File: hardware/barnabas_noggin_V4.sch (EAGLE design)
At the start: 45 parts, among them IC2 LM1117IMPX-5.0, IC3 ATMEGA328P-32MUR, J1 POWER_JACKPTH, J3 USB-mini-90 -SMD, J4 ICSP, SW1 157SW, Y1 16MHZ, Y2 12MHz

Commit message: Updated V4 schematics.
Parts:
- removed F1: FUSE_6V, barnabas_noggin_V4:FUSE_6V
- added F2: FUSE_6V, barnabas_noggin_V4:FUSE_6V
- added JP7: 2.54mm, barnabas_noggin_V4:PINHD-1X6
- added M1, M2, M3, M4: MOUNT_HOLE, barnabas_noggin_V4:MOUNT_HOLE
- added R7, R8, R9: 1K, barnabas_noggin_V4:RESISTOR0603
- added SW2: 157SW, barnabas_noggin_V4:PUSHBUTTON
- added U1: L9110S_DRIVER, barnabas_noggin_V4:L9110S_DRIVER
- R4: device barnabas_noggin_V4:RESISTORX4 -> barnabas_noggin_V4:RESISTOR0603; PARTNO CAY16-102J4LF -> RC0603FR-071KL
- renumbered U$1 to IC1
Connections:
- removed net COM: C4.2, IC1.GND
- removed net N$11: L.A, R4D.1
- removed net N$15: F1.1, J3.VBUS
- new net 5V_PIN: C11.1, C12.1, C13.1, C14.1, C3.1, C5.+, C7.1, F2.2, IC1.VCC, IC3.AVCC, IC3.VCC@1, IC3.VCC@2, J4.2, JP1.3, JP1.4, JP2.3, JP2.4, JP6.4, R1.2, R7.2, R8.2, R9.2
- new net N$10: L.A, R4.1
- net 5V: now also F2.1; no longer C11.1, C12.1, C13.1, C14.1, C3.1, C5.+, C7.1, IC1.VCC, IC3.AVCC, IC3.VCC@1, IC3.VCC@2, J4.2, JP1.3, JP1.4, JP2.3, JP2.4, JP6.4, R1.2, R4A.2, R4B.2
- net D12/MISO: now also JP7.1
- net D13/SCK: now also R4.2; no longer R4D.2
- net D2: now also SW2.1
- net GND: now also C4.2, IC1.GND, SW2.2
- net N$3: now also R7.1; no longer R4C.1
- net N$7: now also R8.1; no longer R4A.1
- net N$9: now also R9.1; no longer R4B.1
- net VOUT: no longer R4C.2
- net VUSB: now also J3.VBUS; no longer F1.2
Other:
- note added: "DC Driver Connector"
- moved on the sheet: C4, D1, D2, JP3, JP4, JP5, JP6, PWR

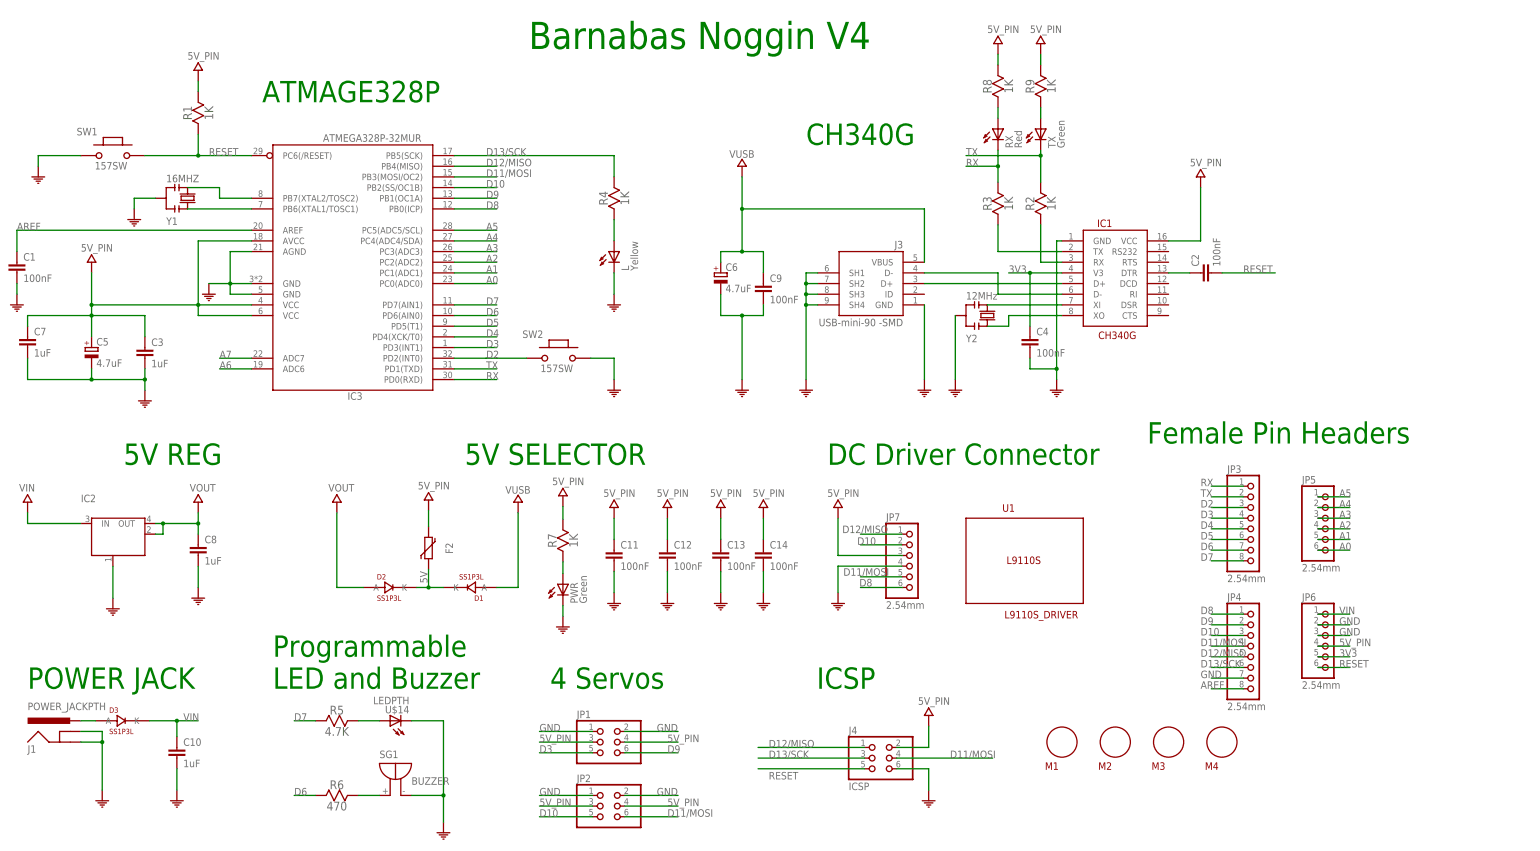
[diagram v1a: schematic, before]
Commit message: Added 3.3V regulator.
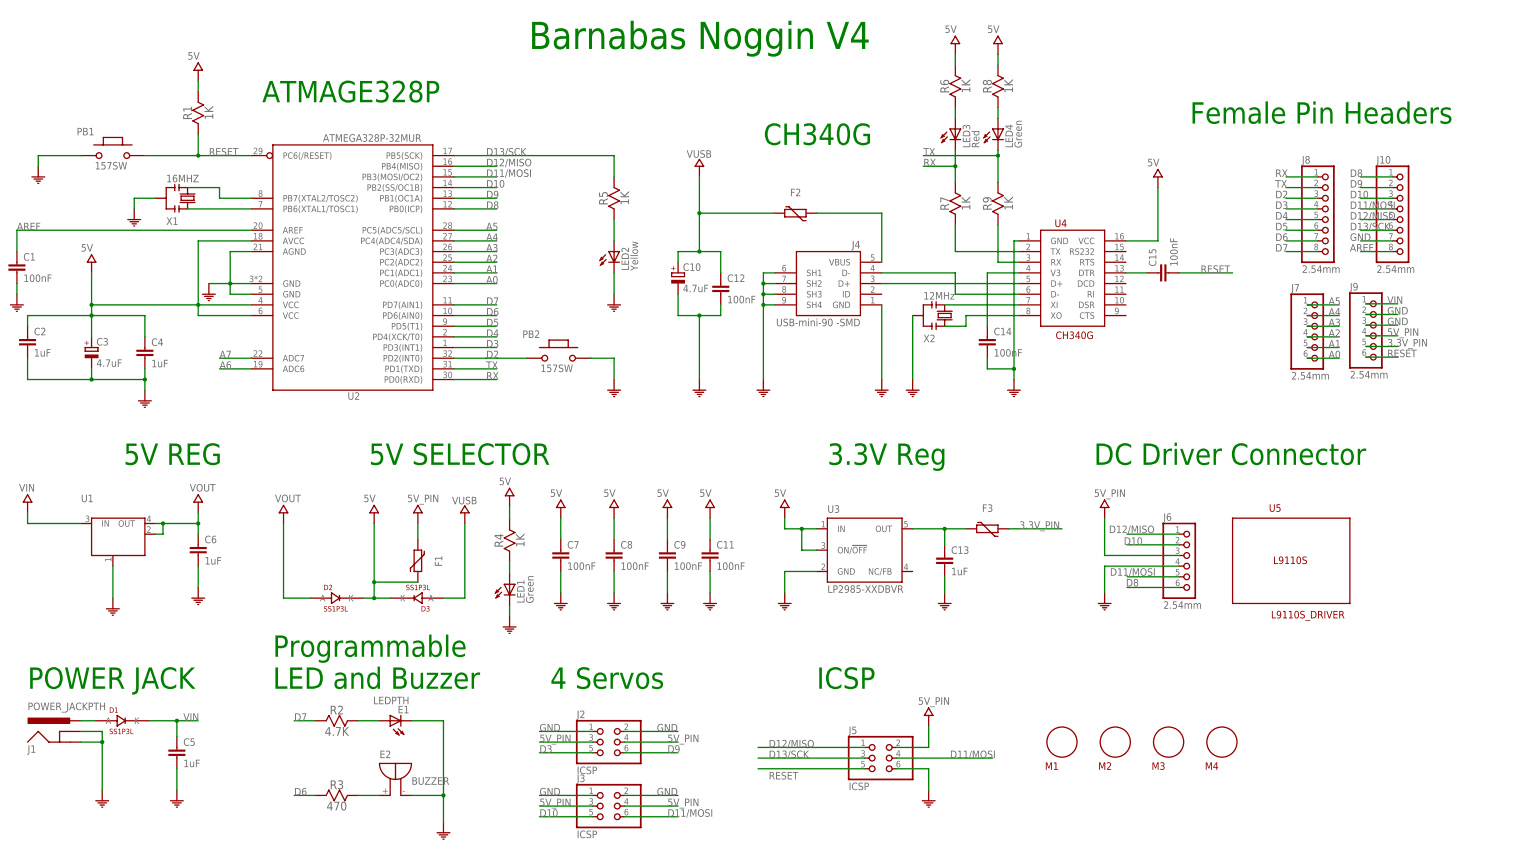
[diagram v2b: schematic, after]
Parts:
- removed IC1: CH340G, barnabas_noggin_V4:CH340G
- removed IC2: LM1117IMPX-5.0, barnabas_noggin_V4:LM1117
- removed JP2: (no value), barnabas_noggin_V4:CONNECTOR_2X3
- removed JP3, JP4: 2.54mm, barnabas_noggin_V4:PINHD-1X8
- removed JP5, JP6, JP7: 2.54mm, barnabas_noggin_V4:PINHD-1X6
- removed PWR, TX: Green, barnabas_noggin_V4:LED_GREEN
- removed RX: Red, barnabas_noggin_V4:LED_RED
- removed Y2: 12MHz, barnabas_noggin_V4:CRYSTAL_12MHZ
- added C15: 100nF, barnabas_noggin_V4:CAPACITOR_100NF_0603
- added F1, F3: FUSE_6V, barnabas_noggin_V4:FUSE_6V
- added J10, J8: 2.54mm, barnabas_noggin_V4:PINHD-1X8
- added J5: ICSP, barnabas_noggin_V4:CONNECTOR_2X3
- added J6, J7, J9: 2.54mm, barnabas_noggin_V4:PINHD-1X6
- added LED1, LED4: Green, barnabas_noggin_V4:LED_GREEN
- added LED3: Red, barnabas_noggin_V4:LED_RED
- added U3: LP2985-XXDBVR, barnabas_noggin_V4:LP2985-XXDBVR
- added U4: CH340G, barnabas_noggin_V4:CH340G
- added U5: L9110S_DRIVER, barnabas_noggin_V4:L9110S_DRIVER
- added X2: 12MHz, barnabas_noggin_V4:CRYSTAL_12MHZ
- C10, C3: value 1uF -> 4.7uF; device barnabas_noggin_V4:CAPACITOR_1UF_0603 -> barnabas_noggin_V4:CAPACITOR_4.7UF; PARTNO CC0603KRX5R8BB105 -> CL31A475KOHNNNE
- C13, C2, C4: value 100nF -> 1uF; device barnabas_noggin_V4:CAPACITOR_100NF_0603 -> barnabas_noggin_V4:CAPACITOR_1UF_0603; PARTNO CC0603ZRY5V9BB104 -> CC0603KRX5R8BB105
- C5, C6: value 4.7uF -> 1uF; device barnabas_noggin_V4:CAPACITOR_4.7UF -> barnabas_noggin_V4:CAPACITOR_1UF_0603; PARTNO CL31A475KOHNNNE -> CC0603KRX5R8BB105
- C7, C8: value 1uF -> 100nF; device barnabas_noggin_V4:CAPACITOR_1UF_0603 -> barnabas_noggin_V4:CAPACITOR_100NF_0603; PARTNO CC0603KRX5R8BB105 -> CC0603ZRY5V9BB104
- J2: value (none) -> ICSP
- J3: value USB-mini-90 -SMD -> ICSP; device barnabas_noggin_V4:CONNECTOR_USB_MINI-B -> barnabas_noggin_V4:CONNECTOR_2X3
- J4: value ICSP -> USB-mini-90 -SMD; device barnabas_noggin_V4:CONNECTOR_2X3 -> barnabas_noggin_V4:CONNECTOR_USB_MINI-B
- R2: value 1K -> 4.7K; device barnabas_noggin_V4:RESISTOR0603 -> barnabas_noggin_V4:RESISTOR; PARTNO RC0603FR-071KL -> (none)
- R3: value 1K -> 470; device barnabas_noggin_V4:RESISTOR0603 -> barnabas_noggin_V4:RESISTOR; PARTNO RC0603FR-071KL -> (none)
- R5: value 4.7K -> 1K; device barnabas_noggin_V4:RESISTOR -> barnabas_noggin_V4:RESISTOR0603; PARTNO (none) -> RC0603FR-071KL
- R6: value 470 -> 1K; device barnabas_noggin_V4:RESISTOR -> barnabas_noggin_V4:RESISTOR0603; PARTNO (none) -> RC0603FR-071KL
- U1: value L9110S_DRIVER -> LM1117IMPX-5.0; device barnabas_noggin_V4:L9110S_DRIVER -> barnabas_noggin_V4:LM1117; PARTNO (none) -> LM1117IMPX-5.0/NOPB
- renumbered IC3 to U2, JP1 to J2, L to LED2, SG1 to E2, SW1 to PB1, SW2 to PB2, U$14 to E1, Y1 to X1
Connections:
- removed net 3V3: C4.1, IC1.V3, JP6.5
- new net 3.3V: C13.1, F3.2, U3.OUT
- new net 3.3V_PIN: F3.1, J9.5
- new net N$11: C14.1, U4.V3
- new net N$17: F2.1, J4.VBUS
- net 5V: now also C11.1, C2.1, C3.+, C4.1, C7.1, C8.1, C9.1, D3.K, F1.1, R1.2, R4.2, R6.2, R8.2, U2.AVCC, U2.VCC@1, U2.VCC@2, U3.IN, U3.ON/!OFF, U4.VCC; no longer D1.K, F2.1
- net 5V_PIN: now also F1.2, J3.3, J3.4, J5.2, J6.3, J9.4; no longer C11.1, C12.1, C13.1, C14.1, C3.1, C5.+, C7.1, F2.2, IC1.VCC, J4.2, JP2.3, JP2.4, JP6.4, R1.2, R7.2, R8.2, R9.2, U2.AVCC, U2.VCC@1, U2.VCC@2
- net A0: now also J7.6; no longer JP5.6
- net A1: now also J7.5; no longer JP5.5
- net A2: now also J7.4; no longer JP5.4
- net A3: now also J7.3; no longer JP5.3
- net A4: now also J7.2; no longer JP5.2
- net A5: now also J7.1; no longer JP5.1
- net AREF: now also J10.8; no longer JP4.8
- net D10: now also J10.3, J3.5, J6.2; no longer JP2.5, JP4.3
- net D11/MOSI: now also J10.4, J3.6, J5.4, J6.5; no longer J4.4, JP2.6, JP4.4
- net D12/MISO: now also J10.5, J5.1, J6.1; no longer J4.1, JP4.5, JP7.1
- net D13/SCK: now also J10.6, J5.3, R5.2; no longer J4.3, JP4.6, R4.2
- net D2: now also J8.3; no longer JP3.3
- net D3: now also J8.4; no longer JP3.4
- net D4: now also J8.5; no longer JP3.5
- net D5: now also J8.6; no longer JP3.6
- net D6: now also J8.7, R3.1; no longer JP3.7, R6.1
- net D7: now also J8.8, R2.1; no longer JP3.8, R5.1
- net D8: now also J10.1, J6.6; no longer JP4.1
- net D9: now also J10.2; no longer JP4.2
- net GND: now also C10.-, C2.2, C3.-, C5.2, C6.2, J10.7, J3.1, J3.2, J4.GND, J4.SH1, J4.SH2, J4.SH3, J4.SH4, J5.6, J6.4, J9.2, J9.3, LED1.C, U1.GND/ADJ, U3.GND, U4.GND, X2.2; no longer C10.2, C3.2, C5.-, C6.-, IC1.GND, IC2.GND/ADJ, J3.GND, J3.SH1, J3.SH2, J3.SH3, J3.SH4, J4.6, JP2.1, JP2.2, JP4.7, JP6.2, JP6.3, PWR.C, Y2.2
- net N$10: now also R5.1; no longer R4.1
- net N$12: now also U4.XO, X2.1; no longer IC1.XO, Y2.1
- net N$13: now also J4.D+, U4.D+; no longer IC1.D+, J3.D+
- net N$14: now also J4.D-, U4.D-; no longer IC1.D-, J3.D-
- net N$16: now also D1.A; no longer D3.A
- net N$18: now also R2.2; no longer R5.2
- net N$19: now also R3.2; no longer R6.2
- net N$3: now also LED1.A, R4.1; no longer PWR.A, R7.1
- net N$4: now also C15.1, U4.DTR; no longer C2.1, IC1.DTR
- net N$5: now also U4.XI, X2.3; no longer IC1.XI, Y2.3
- net N$6: now also R7.1, U4.TX; no longer IC1.TX, R3.1
- net N$7: now also LED3.A, R6.1; no longer R8.1, RX.A
- net N$8: now also R9.1, U4.RX; no longer IC1.RX, R2.1
- net N$9: now also LED4.A, R8.1; no longer R9.1, TX.A
- net RESET: now also C15.2, J5.5, J9.6; no longer C2.2, J4.5, JP6.6
- net RX: now also J8.1, LED3.C, R7.2; no longer JP3.1, R3.2, RX.C
- net TX: now also J8.2, LED4.C, R9.2; no longer JP3.2, R2.2, TX.C
- net VIN: now also C5.1, D1.K, J9.1, U1.IN; no longer C10.1, D3.K, IC2.IN, JP6.1
- net VOUT: now also C6.1, U1.OUT, U1.OUT@1; no longer C8.1, IC2.OUT, IC2.OUT@1
- net VUSB: now also C10.+, C12.1, D3.A, F2.2; no longer C6.+, C9.1, D1.A, J3.VBUS
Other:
- note added: "3.3V Reg"
- moved on the sheet: C11, C12, C13, C14, C2, C4, C7, C8, C9, D1, D2, D3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
